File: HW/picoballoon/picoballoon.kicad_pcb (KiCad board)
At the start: 4 copper layers, 50 x 50 mm, 68 parts, among them J1 EXT_DEBUGGER, U1 Si4461, U2 MPL3115A2, U4 MCP9802, U5 MAX-M10S, U6 OPA333xxDBV, Y1 30M

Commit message: picoballoon pcb
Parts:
- added ?: , , F.Cu at (148.4, 128.9)
- added ?: , , F.Cu at (147.4, 128.9)
- added ?: , , F.Cu at (147.4, 129.9)
- added ?: , , F.Cu at (146.3, 128.9)
- added ?: , , F.Cu at (147.4, 127.8)
- added AE1: Antenna, Library:RECE20369001E01, F.Cu at (102.8, 111.7)
- added AE2: Antenna, Library:RECE20369001E01, F.Cu at (153.9, 146.4)
- added C12: 100n, Capacitor_SMD:C_0603_1608Metric_Pad1.08x0.95mm_HandSolder, F.Cu at (115.7, 126.2)
- added R6: 10k, Resistor_SMD:R_0603_1608Metric_Pad0.98x0.95mm_HandSolder, F.Cu at (115.7, 127.8)
- C14: value XX -> 10 F
- moved C16 75.0 mm to (154.3, 128.4), turned to 90 degrees
- moved C10 73.1 mm to (152.6, 128.4), turned to 90 degrees
- moved C34 72.4 mm to (156.4, 141.8), turned to 90 degrees
- moved C8 71.2 mm to (151.0, 128.4), turned to 90 degrees
- moved C33 69.0 mm to (152.9, 140.1), turned to 90 degrees
- moved L3 68.0 mm to (152.1, 137.5)
- moved L6 67.4 mm to (155.5, 139.2)
- moved C17 66.3 mm to (146.1, 136.7), turned to 90 degrees
- moved C32 65.7 mm to (149.5, 138.4), turned to 90 degrees
- moved C31 65.0 mm to (144.4, 134.9), turned to -90 degrees
- moved C6 64.5 mm to (105.5, 126.9), turned to -90 degrees
- moved L2 61.6 mm to (145.3, 132.3), turned to 180 degrees
- moved L7 60.3 mm to (148.7, 132.3), turned to 180 degrees
- moved L8 60.2 mm to (148.7, 135.8)
- moved C4 59.0 mm to (118.5, 111.9), turned to 90 degrees
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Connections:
- C31 pad 1: Net-(U1-TX) -> Net-(C31-Pad1)
- C31 pad 2: Net-(C31-Pad2) -> Net-(C17-Pad2)
- L2 pad 1: Net-(C31-Pad2) -> Net-(U1-TX)
- L2 pad 2: Net-(C17-Pad2) -> Net-(C31-Pad1)
- Y1 pad 3: (no net) -> GND
- Y1 pad 4: (no net) -> GND
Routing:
- net +3.3V: track 0.00 -> 100.5 mm, vias 0 -> 28
- net GND: track 0.00 -> 29.9 mm, vias 0 -> 403
- net +U_SC: track 0.00 -> 28.2 mm
- net /SCL_SENS: track 0.00 -> 26.3 mm
- net /nIRQ: track 0.00 -> 25.8 mm
- net /SDA_SENS: track 0.00 -> 24.8 mm
- net /VDD_CORE: track 0.00 -> 24.8 mm, vias 0 -> 2
- net /MOSI: track 0.00 -> 22.5 mm, vias 0 -> 2
- net /GNSS_RESET: track 0.00 -> 22.1 mm, vias 0 -> 2
- net /MISO: track 0.00 -> 22.0 mm, vias 0 -> 2
- net /SCLK: track 0.00 -> 21.2 mm
- net /GNSS_SDA: track 0.00 -> 20.6 mm
- net /ADC: track 0.00 -> 20.3 mm
- net /RESET: track 0.00 -> 19.4 mm
- net /ISP: track 0.00 -> 18.7 mm
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- added copper zone on In2.Cu, net +3.3V
- added copper zone on B.Cu, net GND
- added copper zone on F.Cu, net GND
- added copper zone on In1.Cu, net GND
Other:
- board size 50 x 50 mm -> 58.4 x 42 mm

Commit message: minor fixes
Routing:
- net GND: vias 403 -> 408
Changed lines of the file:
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@@
 		(tags "resistor handsolder")
 		(property "Reference" "R13"
-			(at -3.13 -0.03 90)
+			(at -0.44 1.46 90)
 			(layer "F.SilkS")
 			(effects
@@
 		(tags "SOT TO_SOT_SMD")
 		(property "Reference" "U4"
-			(at -2.6875 -2.4 0)
+			(at -2.3575 -2.44 0)
 			(layer "F.SilkS")
 			(effects
@@
 		(tags "capacitor handsolder")
 		(property "Reference" "C18"
-			(at 1.53 1.49 90)
+			(at 0.44 1.44 90)
 			(layer "F.SilkS")
 			(effects
@@
 		(tags "capacitor handsolder")
 		(property "Reference" "C4"
-			(at 2.8 -0.01 90)
+			(at -2.63 0.0145 90)
 			(layer "F.SilkS")
 			(effects
@@
 		(tags "Connector")
 		(property "Reference" "AE1"
-			(at 2.98 -0.003 180)
+			(at 2.98 -0.6475 180)
 			(layer "F.SilkS")
 			(effects
@@
 		(tags "Power Supply")
 		(property "Reference" "PS1"
-			(at 0.04 2.76 0)
+			(at 0.03 2.28 0)
 			(layer "F.SilkS")
 			(effects
@@
 		(tags "capacitor handsolder")
 		(property "Reference" "C5"
-			(at 2.9 0.04 90)
+			(at -2.54 -0.0555 90)
 			(layer "F.SilkS")
 			(effects
@@
 	)
 	(via
+		(at 145.84 123.9)
+		(size 0.6)
+		(drill 0.3)
+		(layers "F.Cu" "B.Cu")
+		(free yes)
+		(net 1)
+	)
+	(via
 		(at 151.26 139.72)
 		(size 0.6)
@@
 	)
 	(via
-		(at 128.75 127)
+		(at 127.9 126.8)
 		(size 0.6)
 		(drill 0.3)
@@
 	)
 	(via
+		(at 137.77 120.93)
+		(size 0.6)
+		(drill 0.3)
+		(layers "F.Cu" "B.Cu")
+		(free yes)
+		(net 1)
+	)
+	(via
 		(at 104 108.75)
 		(size 0.6)
@@
 	)
 	(via
+		(at 133.59 120.86)
+		(size 0.6)
+		(drill 0.3)
+		(layers "F.Cu" "B.Cu")
+		(free yes)
+		(net 1)
+	)
+	(via
 		(at 112 149.25)
 		(size 0.6)
@@
 	)
 	(via
+		(at 135.35 120.89)
+		(size 0.6)
+		(drill 0.3)
+		(layers "F.Cu" "B.Cu")
+		(free yes)
+		(net 1)
+	)
+	(via
 		(at 101 114.25)
 		(size 0.6)
@@
 		(size 0.6)
 		(drill 0.3)
+		(layers "F.Cu" "B.Cu")
+		(free yes)
+		(net 1)
+	)
+	(via
+		(at 145.26 120.81)
+		(size 0.6)
+		(drill 0.3)

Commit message: test points
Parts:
- added TP1: +3.3VA_TP, TestPoint:TestPoint_Pad_D2.0mm, F.Cu at (112.3, 135.2)
- added TP10: GND, TestPoint:TestPoint_Pad_D2.0mm, F.Cu at (152.0, 114.5)
- added TP2: +3.3V_TP, TestPoint:TestPoint_Pad_D2.0mm, F.Cu at (104.4, 136.2)
- added TP3: ADC, TestPoint:TestPoint_Pad_D2.0mm, F.Cu at (116.8, 139.4)
- added TP4: SDA_TEMP, TestPoint:TestPoint_Pad_D2.0mm, F.Cu at (108.0, 121.9)
- added TP5: SCL_TEMP, TestPoint:TestPoint_Pad_D2.0mm, F.Cu at (103.0, 130.0)
- added TP6: SCLK, TestPoint:TestPoint_Pad_D2.0mm, F.Cu at (151.8, 124.5)
- added TP7: MOSI, TestPoint:TestPoint_Pad_D2.0mm, F.Cu at (151.7, 120.4)
- added TP8: MISO, TestPoint:TestPoint_Pad_D2.0mm, F.Cu at (155.1, 120.4)
- added TP9: GND, TestPoint:TestPoint_Pad_D2.0mm, F.Cu at (142.6, 141.9)
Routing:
- net /MISO: track 22.0 -> 30.1 mm
- net /SCL_TEMP: track 13.2 -> 20.6 mm
- net +3.3V: track 100.5 -> 107.4 mm, vias 28 -> 30
- net /MOSI: track 22.5 -> 27.9 mm
- net +3.3VA: track 10.9 -> 15.8 mm
- net /SCLK: track 21.2 -> 24.6 mm
- net /SDA_TEMP: track 12.8 -> 15.9 mm
- net /ADC: track 20.3 -> 23.1 mm
- net GND: track 29.9 -> 31.5 mm, vias 408 -> 407
- net /nIRQ: track 25.8 -> 27.2 mm, vias 0 -> 2
- net /GNSS_SDA: track 20.6 -> 21.3 mm

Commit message: test points
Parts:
- renumbered C14 to C1, C23 to C10, C24 to C11, C25 to C12, C26 to C13, C27 to C14, C12 to C15, C28 to C16, C29 to C17, C15 to C18, C6 to C19, C7 to C2, C2 to C20, C1 to C21, C3 to C22, C13 to C23, C4 to C24, C5 to C25, C8 to C26, C10 to C27, C16 to C28, C31 to C29, C9 to C3, C17 to C30, C32 to C31, C33 to C32, C34 to C33, C11 to C4, C18 to C5, C19 to C6, C20 to C7, C21 to C8, C22 to C9, L4 to L2, L5 to L3, L7 to L4, L2 to L5, L8 to L6, L3 to L7, L6 to L8, R2 to R1, R13 to R10, R3 to R11, R7 to R12, R8 to R13, R6 to R2, R4 to R3, R5 to R4, R10 to R5, R11 to R6, R9 to R7, R1 to R8, R12 to R9
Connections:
- MCXL14x2 pad 26: unconnected-(MCXL14x2-P2_8-Pad26) -> /SDN
- U1 pad 1: unconnected-(U1-SDN-Pad1) -> /SDN
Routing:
- net /SDN: track 0.00 -> 28.2 mm, vias 0 -> 2
- net GND: track 31.5 -> 29.7 mm, vias 407 -> 405

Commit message: mcxc
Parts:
- removed the ? at (148.4, 128.9)
- removed the ? at (147.4, 128.9)
- removed the ? at (147.4, 129.9)
- removed the ? at (146.3, 128.9)
- removed the ? at (147.4, 127.8)
- removed L2, L3: 4.7u, Inductor_SMD:L_0603_1608Metric_Pad1.05x0.95mm_HandSolder
- removed MCXL14x2: ~, Package_QFP:LQFP-64-1EP_10x10mm_P0.5mm_EP5x5mm
- added ?: , , F.Cu at (141.9, 89.8)
- added ?: , , F.Cu at (143.0, 89.9)
- added ?: , , F.Cu at (143.0, 88.8)
- added ?: , , F.Cu at (144.0, 89.8)
- added ?: , , F.Cu at (143.0, 90.9)
- added C37: 100n, Capacitor_SMD:C_0603_1608Metric_Pad1.08x0.95mm_HandSolder, F.Cu at (148.2, 117.1)
- added IC1: MCXC141VLH, Package_QFP:LQFP-64-1EP_10x10mm_P0.5mm_EP5x5mm, F.Cu at (137.0, 104.6)
- added R14: 1k, Resistor_SMD:R_0603_1608Metric_Pad0.98x0.95mm_HandSolder, F.Cu at (124.0, 105.6)
- added R15: 10k, Resistor_SMD:R_0603_1608Metric_Pad0.98x0.95mm_HandSolder, F.Cu at (145.8, 120.8)
- added R16: 10k, Resistor_SMD:R_0603_1608Metric_Pad0.98x0.95mm_HandSolder, F.Cu at (144.1, 120.8)
- added R17: 1M, Resistor_SMD:R_0603_1608Metric_Pad0.98x0.95mm_HandSolder, F.Cu at (119.2, 118.1)
- added R18: 1M, Resistor_SMD:R_0603_1608Metric_Pad0.98x0.95mm_HandSolder, F.Cu at (120.9, 118.1)
- added R19: 0, Resistor_SMD:R_0603_1608Metric_Pad0.98x0.95mm_HandSolder, F.Cu at (140.6, 117.2)
- AE2: footprint Library:RECE20369001E01 -> Library:BNC_Connector_PCB
- C10, C6, C8: value 100n -> 1u
- C16: value 4.7u -> 100n
- C17: value 4.7u -> xx
- R12, R13: value 1M -> 10k
- moved C19 55.4 mm to (157.1, 106.6), turned to 90 degrees
- moved AE2 55.1 mm to (157.1, 91.3), turned to 90 degrees
- moved U4 49.9 mm to (154.1, 106.6), turned to 180 degrees
- moved R5 49.4 mm to (158.1, 120.1), turned to -90 degrees
- moved TP9 49.0 mm to (110.7, 104.7)
- moved C30 46.7 mm to (150.8, 90.2), turned to 180 degrees
- moved L4 45.3 mm to (146.5, 87.1), turned to -90 degrees
- moved C27 44.5 mm to (138.4, 86.3), turned to 180 degrees
- moved R6 43.6 mm to (151.5, 120.2), turned to -90 degrees
- moved C28 43.5 mm to (138.4, 87.9), turned to 180 degrees
- moved C29 43.4 mm to (149.1, 91.8), turned to 0 degrees
- moved C31 43.2 mm to (152.5, 95.3), turned to 180 degrees
- moved C26 43.1 mm to (142.0, 86.3), turned to 180 degrees
- moved TP6 42.9 mm to (132.0, 86.5)
- moved L5 41.4 mm to (146.6, 90.9), turned to -90 degrees
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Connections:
- AE1 pad 2: GND -> (no net)
- AE1 pad 3: GND -> (no net)
- AE1 pad 4: GND -> (no net)
- AE2 pad 2: GND -> (no net)
- C15 pad 1: /RESET -> +3.3VA
- C16 pad 1: /VDD_CORE -> /RESET
- C17 pad 1: /VDD_CORE_1POV -> Net-(IC1-PTE20)
- J1 pad 2: Net-(J1-Pin_2) -> /SWD_DIO
- J1 pad 4: Net-(J1-Pin_4) -> /SWD_CLK
- J1 pad 6: Net-(J1-Pin_6) -> unconnected-(J1-Pin_6-Pad6)
- J1 pad 7: /ISP -> unconnected-(J1-Pin_7-Pad7)
- J1 pad 8: Net-(J1-Pin_8) -> unconnected-(J1-Pin_8-Pad8)
- R10 pad 1: +3.3V -> /SCL_TEMP
- R10 pad 2: /SCL_SENS -> +3.3V
- R12 pad 1: +U_SC -> Net-(IC1-PTE18)
- R12 pad 2: Net-(U6-+) -> GND
- R13 pad 1: Net-(U6-+) -> +3.3V
- R13 pad 2: GND -> Net-(IC1-PTA4)
- R5 pad 1: +3.3V -> /SDA_SENS
- R5 pad 2: /SDA_TEMP -> +3.3V
- R6 pad 1: +3.3V -> /SCL_SENS
- R6 pad 2: /SCL_TEMP -> +3.3V
- R7 pad 2: /MOSI -> /MISO
- R8 pad 2: /nIRQ -> /MOSI
- R9 pad 1: +3.3V -> /SDA_TEMP
- R9 pad 2: /SDA_SENS -> +3.3V
- TP4 pad 1: /SDA_TEMP -> /GNSS_SDA
- TP5 pad 1: /SCL_TEMP -> /GNSS_SCL
- Y1 pad 3: GND -> (no net)
- Y1 pad 4: GND -> (no net)
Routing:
- net /VDD_CORE: track 24.8 -> 0.00 mm, vias 2 -> 0
- net +3.3V: track 107.0 -> 84.9 mm, vias 30 -> 27
- net /SWD_DIO: track 0.00 -> 20.5 mm, vias 0 -> 2
- net /SWD_CLK: track 0.00 -> 18.7 mm
- net /ISP: track 18.7 -> 0.00 mm
- net /VDD_CORE_1POV: track 15.4 -> 0.00 mm
- net /RESET: track 19.4 -> 6.30 mm
- net /nIRQ: track 27.2 -> 14.7 mm, vias 2 -> 0
- net /MISO: track 30.1 -> 18.4 mm
- net /nSEL: track 18.0 -> 8.54 mm
- net /SCL_TEMP: track 20.6 -> 11.2 mm
- net Net-(IC1-PTE20): track 0.00 -> 9.30 mm
- net /MOSI: track 27.9 -> 18.6 mm
- net /GNSS_SCL: track 18.4 -> 27.4 mm
- net Net-(J1-Pin_2): track 8.68 -> 0.00 mm
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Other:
- board size 58.4 x 42 mm -> 55 x 45 mm

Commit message: gnss antenna
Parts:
- moved TP8 0.40 mm to (131.1, 89.4)
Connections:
- AE1 pad 2: (no net) -> GND
- AE1 pad 3: (no net) -> GND
- AE1 pad 4: (no net) -> GND
- Y1 pad 3: (no net) -> GND
- Y1 pad 4: (no net) -> GND
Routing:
- net /MISO: track 18.4 -> 19.0 mm
- net GND: vias 457 -> 456
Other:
- board size 55 x 45 mm -> 55 x 63 mm
- board text added: "GNSS Antenna"
- board text added: "Vojtech Piroch Picoballoon v1 2024/25"

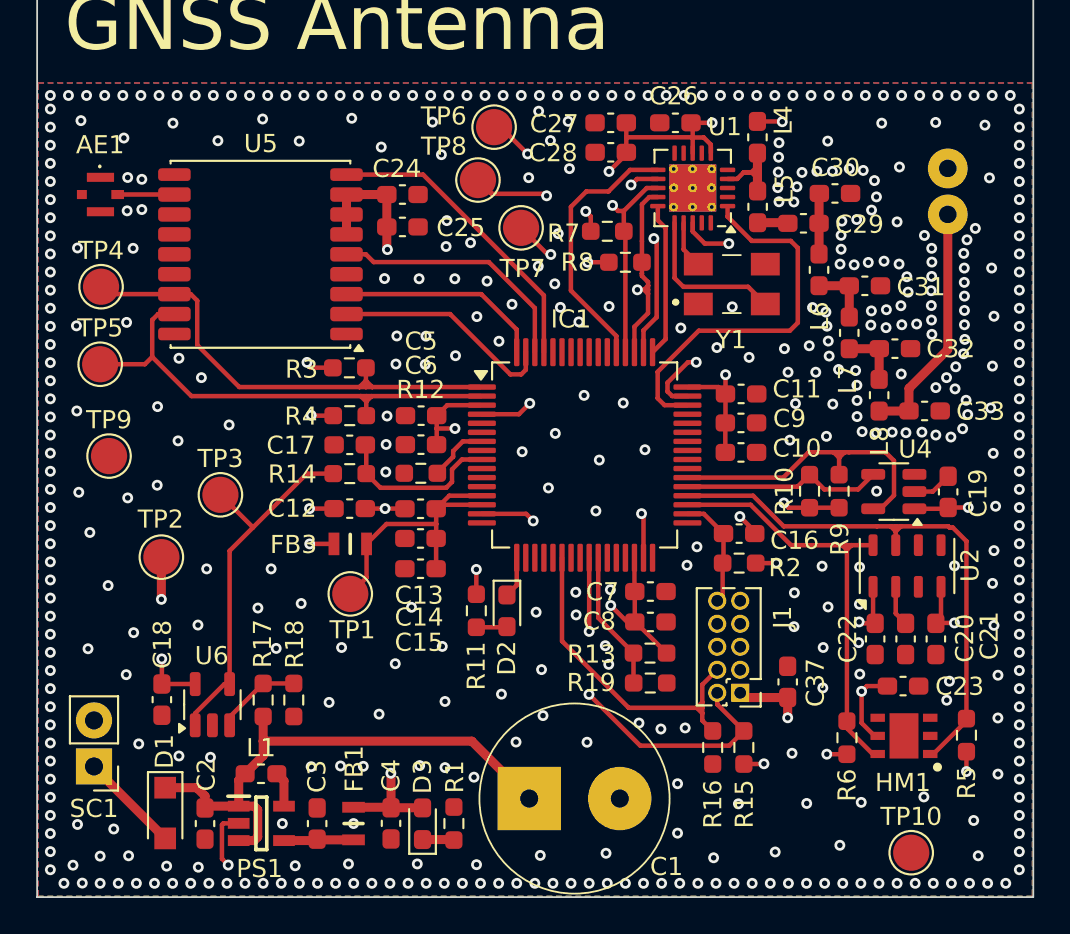
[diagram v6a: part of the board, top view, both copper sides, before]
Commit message: mounting holes
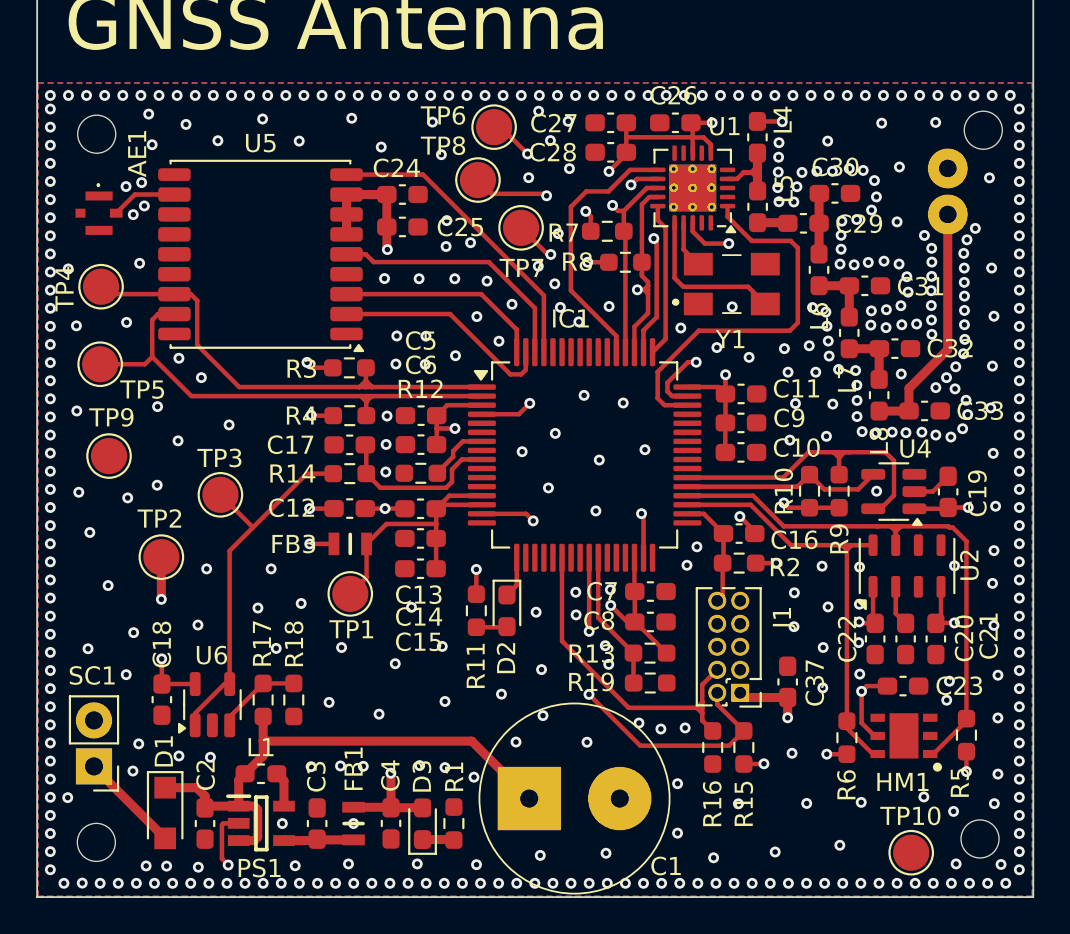
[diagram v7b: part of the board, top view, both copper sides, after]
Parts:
- added H1: MountingHole, MountingHole:MountingHole_2.1mm, F.Cu at (110.0, 126.0)
- added H2: MountingHole, MountingHole:MountingHole_2.1mm, F.Cu at (158.8, 125.8)
- added H3: MountingHole, MountingHole:MountingHole_2.1mm, F.Cu at (159.0, 86.7)
- added H4: MountingHole, MountingHole:MountingHole_2.1mm, F.Cu at (110.1, 86.9)
- moved AE1 1.03 mm to (110.2, 91.2)
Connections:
- AE2 pad 2: (no net) -> GND
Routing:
- net Net-(AE1-A): track 3.13 -> 3.64 mm
- net GND: vias 456 -> 455
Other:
- board text added: "+"
- board text added: "-"
- board text added: "sig"

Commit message: power supply change
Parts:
- added J2: Conn_01x02, Connector_PinHeader_1.27mm:PinHeader_1x02_P1.27mm_Vertical, F.Cu at (127.6, 119.5)
- moved C1 16.4 mm to (120.0, 123.0)
- moved FB1 11.1 mm to (135.4, 124.7)
- moved C4 11.1 mm to (137.4, 124.7)
- moved L1 11.1 mm to (130.2, 121.9)
- moved PS1 11.1 mm to (130.3, 124.7)
- moved R1 11.1 mm to (140.9, 124.7)
- moved C2 11.1 mm to (127.2, 124.7)
- moved C3 11.1 mm to (133.3, 124.7)
- moved D3 11.1 mm to (139.2, 124.7)
- moved TP2 3.39 mm to (110.7, 108.6)
- moved D1 3.02 mm to (113.2, 121.4), turned to 90 degrees
- moved C18 2.90 mm to (113.6, 115.2)
- moved R17 2.90 mm to (119.2, 115.2)
- moved R18 2.90 mm to (120.8, 115.2)
- moved U6 2.90 mm to (116.3, 115.5)
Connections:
- AE1 pad 2: GND -> (no net)
- AE1 pad 3: GND -> (no net)
- AE1 pad 4: GND -> (no net)
- AE2 pad 2: GND -> (no net)
- C1 pad 1: +U_SC -> +U_SC1
- D1 pad 1: +U_SC -> +U_SC1
- Y1 pad 3: GND -> (no net)
- Y1 pad 4: GND -> (no net)
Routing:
- net +U_SC1: track 0.00 -> 14.6 mm
- net +U_SC: track 30.2 -> 22.5 mm
- net /ADC: track 20.6 -> 18.6 mm
- net Net-(D1-A): track 5.60 -> 4.06 mm
- net GND: track 23.9 -> 22.8 mm, vias 455 -> 453
